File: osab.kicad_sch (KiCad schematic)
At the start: 99 parts, among them CON1 TF-01A, CON2 PJ-3420-A-SMT, CON3 TYPE-C-31-M-12, Q1 BC847B, Q2 BC847B, SW1 PPP, SW10 RESET, SW11 Torch, SW2 VOL-, SW3 VOL+, SW4 CHAP-, SW5 CHAP+, SW6 OT/NT, SW7 BOOK-, SW8 BOOK+, SW9 BUTTON_LOCK, U1 VS1000, U2 ME6211C33M5G-N, U3 CAT25640, U4 TP4055, U5 MF5853CS, U6 PAM8302AAS, U7 MF5853CS, Y1 12MHz

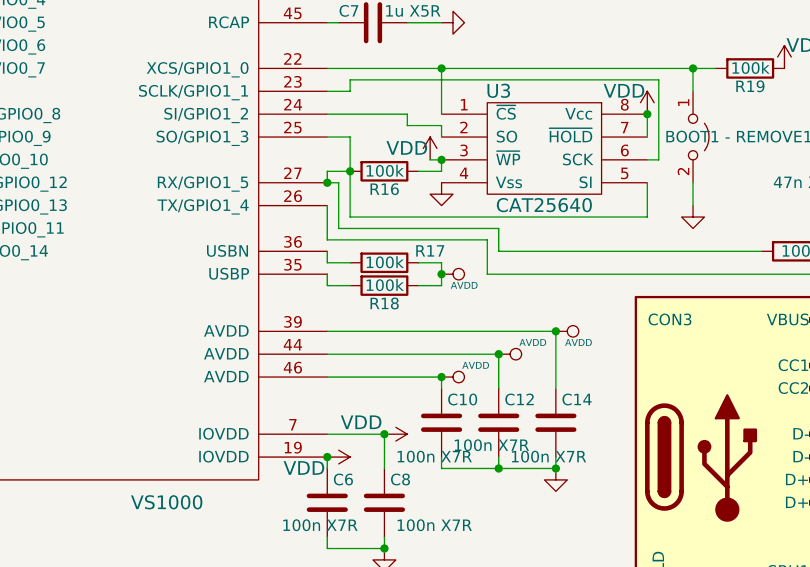
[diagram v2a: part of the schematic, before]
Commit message: production: Changed USB resistors from 100k to 1m as per datasheet
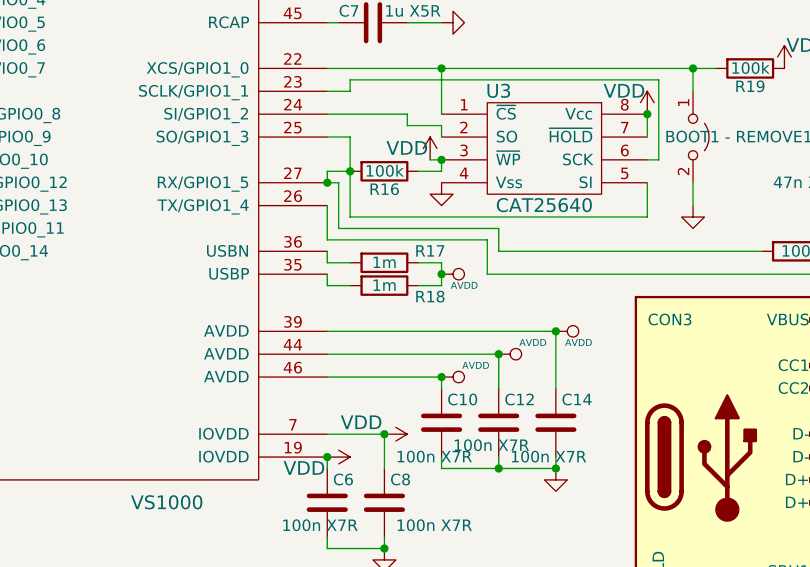
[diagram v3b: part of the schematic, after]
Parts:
- R17, R18: value 100k -> 1m; Link https://lcsc.com/product-detail/Chip-Resistor-Surface-Mount_Viking-Tech-ARG03FTC1003_C217682.html -> https://lcsc.com/product-detail/Chip-Resistor-Surface-Mount_Viking-Tech-AR03FTC1004_C234360.html; MPN ARG03FTC1003 -> AR03FTC1004
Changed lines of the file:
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@@
-    (pin "2")
-  )
-  (symbol (lib_id "Device:R") (at 137.16 113.03 270) (unit 1)
-    (in_bom yes) (on_board yes)
-    (property "Reference" "R17" (id 0) (at 142.24 111.76 90))
-    (property "Value" "100k" (id 1) (at 137.16 113.03 90))
-    (property "Footprint" "Resistor_SMD:R_0603_1608Metric" (id 2) (at 137.16 111.252 90)
-      (effects (font (size 1.27 1.27)) hide)
-    )
-    (property "Datasheet" "https://datasheet.lcsc.com/lcsc/1811091512_Viking-Tech-ARG03FTC1003_C217682.pdf" (id 3) (at 137.16 113.03 0)
-      (effects (font (size 1.27 1.27)) hide)
-    )
-    (property "3D-model" "Included in KiCad" (id 4) (at 137.16 113.03 0)
-      (effects (font (size 1.27 1.27)) hide)
-    )
-    (property "Link" "https://lcsc.com/product-detail/Chip-Resistor-Surface-Mount_Viking-Tech-ARG03FTC1003_C217682.html" (id 5) (at 137.16 113.03 0)
-      (effects (font (size 1.27 1.27)) hide)
-    )
-    (property "MPN" "ARG03FTC1003" (id 6) (at 137.16 113.03 0)
-      (effects (font (size 1.27 1.27)) hide)
-    )
-    (pin "1")
-    (pin "2")
-  )
-  (symbol (lib_id "Device:R") (at 137.16 115.57 270) (unit 1)
-    (in_bom yes) (on_board yes)
-    (property "Reference" "R18" (id 0) (at 137.16 117.602 90))
-    (property "Value" "100k" (id 1) (at 137.16 115.57 90))
-    (property "Footprint" "Resistor_SMD:R_0603_1608Metric" (id 2) (at 137.16 113.792 90)
-      (effects (font (size 1.27 1.27)) hide)
-    )
-    (property "Datasheet" "https://datasheet.lcsc.com/lcsc/1811091512_Viking-Tech-ARG03FTC1003_C217682.pdf" (id 3) (at 137.16 115.57 0)
-      (effects (font (size 1.27 1.27)) hide)
-    )
-    (property "3D-model" "Included in KiCad" (id 4) (at 137.16 115.57 0)
-      (effects (font (size 1.27 1.27)) hide)
-    )
-    (property "Link" "https://lcsc.com/product-detail/Chip-Resistor-Surface-Mount_Viking-Tech-ARG03FTC1003_C217682.html" (id 5) (at 137.16 115.57 0)
-      (effects (font (size 1.27 1.27)) hide)
-    )
-    (property "MPN" "ARG03FTC1003" (id 6) (at 137.16 115.57 0)
-      (effects (font (size 1.27 1.27)) hide)
-    )
-    (pin "1")
     (pin "2")
   )
@@
     (pin "1")
   )
+  (symbol (lib_id "Device:R") (at 137.16 115.57 270) (unit 1)
+    (in_bom yes) (on_board yes)
+    (property "Reference" "R18" (id 0) (at 142.24 116.84 90))
+    (property "Value" "1m" (id 1) (at 137.16 115.57 90))
+    (property "Footprint" "Resistor_SMD:R_0603_1608Metric" (id 2) (at 137.16 113.792 90)
+      (effects (font (size 1.27 1.27)) hide)
+    )
+    (property "Datasheet" "https://datasheet.lcsc.com/lcsc/1912111437_Viking-Tech-AR03FTC1004_C234360.pdf" (id 3) (at 137.16 115.57 0)
+      (effects (font (size 1.27 1.27)) hide)
+    )
+    (property "3D-model" "Included in KiCad" (id 4) (at 137.16 115.57 0)
+      (effects (font (size 1.27 1.27)) hide)
+    )
+    (property "Link" "https://lcsc.com/product-detail/Chip-Resistor-Surface-Mount_Viking-Tech-AR03FTC1004_C234360.html" (id 5) (at 137.16 115.57 0)
+      (effects (font (size 1.27 1.27)) hide)
+    )
+    (property "MPN" "AR03FTC1004" (id 6) (at 137.16 115.57 0)
+      (effects (font (size 1.27 1.27)) hide)
+    )
+    (pin "1")
+    (pin "2")
+  )
   (symbol (lib_id "Transistor_BJT:BC850") (at 118.11 185.42 0) (unit 1)
     (in_bom yes) (on_board yes)
@@
     (pin "8")
   )
+  (symbol (lib_id "Device:R") (at 137.16 113.03 270) (unit 1)
+    (in_bom yes) (on_board yes)
+    (property "Reference" "R17" (id 0) (at 142.24 111.76 90))
+    (property "Value" "1m" (id 1) (at 137.16 113.03 90))
+    (property "Footprint" "Resistor_SMD:R_0603_1608Metric" (id 2) (at 137.16 111.252 90)
+      (effects (font (size 1.27 1.27)) hide)
+    )
+    (property "Datasheet" "https://datasheet.lcsc.com/lcsc/1912111437_Viking-Tech-AR03FTC1004_C234360.pdf" (id 3) (at 137.16 113.03 0)
+      (effects (font (size 1.27 1.27)) hide)
+    )
+    (property "3D-model" "Included in KiCad" (id 4) (at 137.16 113.03 0)
+      (effects (font (size 1.27 1.27)) hide)
+    )
+    (property "Link" "https://lcsc.com/product-detail/Chip-Resistor-Surface-Mount_Viking-Tech-AR03FTC1004_C234360.html" (id 5) (at 137.16 113.03 0)
+      (effects (font (size 1.27 1.27)) hide)
+    )
+    (property "MPN" "AR03FTC1004" (id 6) (at 137.16 113.03 0)
+      (effects (font (size 1.27 1.27)) hide)
+    )
+    (pin "1")
+    (pin "2")
+  )
   (symbol (lib_id "Device:FerriteBead_Small") (at 259.08 78.74 90) (unit 1)
     (in_bom yes) (on_board yes)
@@
       (reference "R16") (unit 1) (value "100k") (footprint "Resistor_SMD:R_0603_1608Metric")
     )
-    (path "/00000000-0000-0000-0000-00005811fb70"
-      (reference "R17") (unit 1) (value "100k") (footprint "Resistor_SMD:R_0603_1608Metric")
-    )
-    (path "/00000000-0000-0000-0000-00005811fcec"
-      (reference "R18") (unit 1) (value "100k") (footprint "Resistor_SMD:R_0603_1608Metric")
+    (path "/f6723e16-11a1-40ca-a3aa-0182b869f65f"
+      (reference "R17") (unit 1) (value "1m") (footprint "Resistor_SMD:R_0603_1608Metric")
+    )
+    (path "/8408e127-31e9-4f78-b888-00a3ef9bcad9"
+      (reference "R18") (unit 1) (value "1m") (footprint "Resistor_SMD:R_0603_1608Metric")
     )
     (path "/00000000-0000-0000-0000-000058122f09"
